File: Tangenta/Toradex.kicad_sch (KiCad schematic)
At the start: 20 parts, among them J17 2309410-1, J30 Conn_01x02_Pin, J31 Conn_01x09_Pin, J32 Conn_02x03_Odd_Even, Q3 BSS138, T1 NTZD3154NT1G

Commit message: Headers.
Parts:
- added J33, J34: Conn_01x05_Pin, Connector_PinHeader_2.54mm:PinHeader_1x05_P2.54mm_Vertical, symbol Connector:Conn_01x05_Pin
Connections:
- net GNDREF: now also J33.1 (Pin_1), J34.1 (Pin_1)
- net SPI_1_CLK: now reaches J17.196
- net SPI_1_CLK: now also J33.2 (Pin_2)
- net SPI_1_MISO: now reaches J17.198
- net SPI_1_MISO: now also J33.3 (Pin_3)
- net SPI_1_MOSI: now reaches J17.200
- net SPI_1_MOSI: now also J33.4 (Pin_4)
- net SPI_1_CS: now reaches J17.202
- net SPI_1_CS: now also J33.5 (Pin_5)
- net GPIO_1: now reaches J17.206
- net GPIO_1: now also J34.2 (Pin_2)
- net GPIO_2: now reaches J17.208
- net GPIO_2: now also J34.3 (Pin_3)
- net GPIO_3: now reaches J17.210
- net GPIO_3: now also J34.4 (Pin_4)
- net GPIO_4: now reaches J17.212
- net GPIO_4: now also J34.5 (Pin_5)
- no-connect marks 167 -> 159

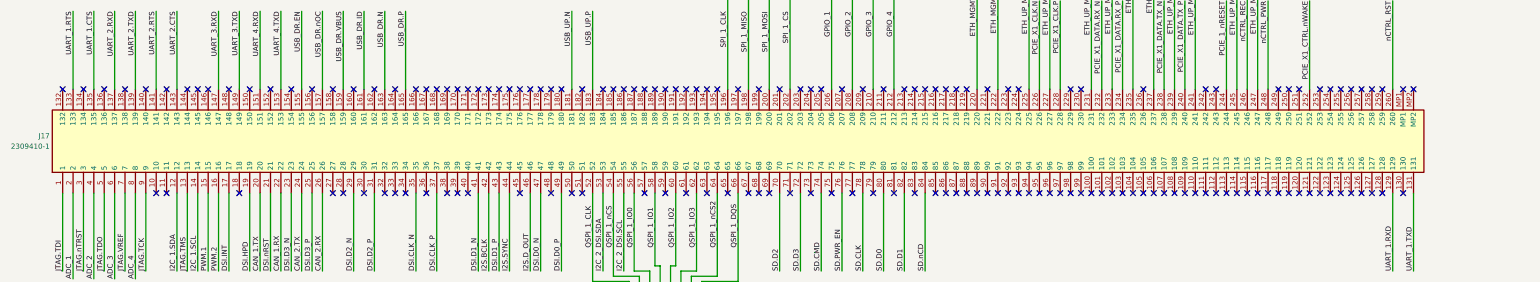
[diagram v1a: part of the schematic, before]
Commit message: SoM power and GND schematic and routing, TBD: power planes
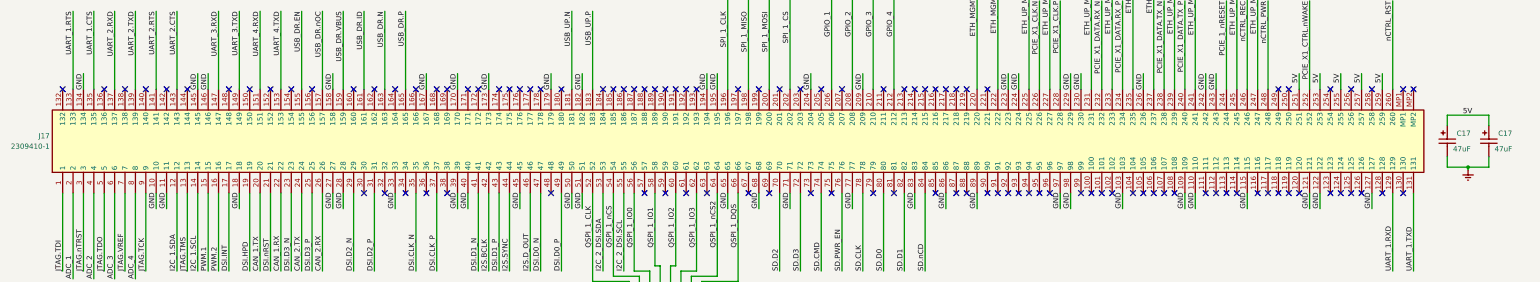
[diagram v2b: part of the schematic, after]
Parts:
- added C17 (x2): 47uF, CAP_TANTAL_A:CAP_TANTAL_A, symbol CAP_TANTAL_A:CA45-A-6_3V-47UF-K
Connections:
- net 5V: now also J17.251, J17.253, J17.255, J17.257, J17.259, C17.1, C17.1
- net GNDREF: now also J17.10, J17.103, J17.109, J17.11, J17.110, J17.115, J17.121, J17.122, J17.127, J17.134, J17.145, J17.146, J17.158, J17.167, J17.170, J17.173, J17.179, J17.18, J17.182, J17.194, J17.195, J17.204, J17.209, J17.223, J17.224, J17.229, J17.230, J17.236, J17.242, J17.243, J17.27, J17.28, J17.33, J17.39, J17.40, J17.45, J17.50, J17.51, J17.65, J17.68, J17.71, J17.77, J17.83, J17.86, J17.89, J17.97, J17.98, C17.2, C17.2
- no-connect marks 159 -> 107

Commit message: Libraries exported from global to project.
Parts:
- C17: symbol CAP_TANTAL_A:CA45-A-6_3V-47UF-K -> CholaSymbolsPrjLib:CA45-A-6_3V-47UF-K
- H15, H16, H17, H18: symbol Mechanical:MountingHole -> CholaSymbolsPrjLib:MountingHole
- J17: symbol SODIMM_DDR4:2309410-1 -> CholaSymbolsPrjLib:2309410-1
- J30: symbol Connector:Conn_01x02_Pin -> CholaSymbolsPrjLib:Conn_01x02_Pin
- J31: symbol Connector:Conn_01x09_Pin -> CholaSymbolsPrjLib:Conn_01x09_Pin
- J32: symbol Connector_Generic:Conn_02x03_Odd_Even -> CholaSymbolsPrjLib:Conn_02x03_Odd_Even
- J33, J34: symbol Connector:Conn_01x05_Pin -> CholaSymbolsPrjLib:Conn_01x05_Pin
- Q3: symbol Transistor_FET:BSS138 -> CholaSymbolsPrjLib:BSS138
- R2: symbol Device:R_Small_US -> CholaSymbolsPrjLib:R_Small_US
- T1: symbol NTZD3154NT1G:NTZD3154NT1G -> CholaSymbolsPrjLib:NTZD3154NT1G
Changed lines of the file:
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@@
     (effects (font (size 1.27 1.27)) (justify left))
   )
-  (symbol (lib_id "Device:R_Small_US") (at 289.56 72.39 180) (unit 1)
+  (symbol (lib_id "CholaSymbolsPrjLib:R_Small_US") (at 289.56 72.39 180) (unit 1)
     (in_bom yes) (on_board yes) (dnp no)
     (property "Reference" "R2" (at 288.29 71.12 0)
@@
     )
   )
-  (symbol (lib_id "Mechanical:MountingHole") (at 281.94 260.35 0) (unit 1)
+  (symbol (lib_id "CholaSymbolsPrjLib:MountingHole") (at 281.94 260.35 0) (unit 1)
     (in_bom yes) (on_board yes) (dnp no)
     (property "Reference" "H15" (at 284.48 260.35 0)
@@
     )
   )
-  (symbol (lib_id "Transistor_FET:BSS138") (at 62.23 246.38 270) (unit 1)
+  (symbol (lib_id "CholaSymbolsPrjLib:BSS138") (at 62.23 246.38 270) (unit 1)
     (in_bom yes) (on_board yes) (dnp no)
     (property "Reference" "Q3" (at 64.77 243.84 90)
@@
     )
   )
-  (symbol (lib_id "Mechanical:MountingHole") (at 281.94 275.59 0) (unit 1)
+  (symbol (lib_id "CholaSymbolsPrjLib:MountingHole") (at 281.94 275.59 0) (unit 1)
     (in_bom yes) (on_board yes) (dnp no)
     (property "Reference" "H18" (at 284.48 275.59 0)
@@
     )
   )
-  (symbol (lib_id "Device:R_Small_US") (at 49.53 242.57 180) (unit 1)
+  (symbol (lib_id "CholaSymbolsPrjLib:R_Small_US") (at 49.53 242.57 180) (unit 1)
     (in_bom yes) (on_board yes) (dnp no)
     (property "Reference" "R2" (at 48.26 241.3 0)
@@
     )
   )
-  (symbol (lib_id "Connector:Conn_01x02_Pin") (at 344.805 77.47 90) (mirror x) (unit 1)
+  (symbol (lib_id "CholaSymbolsPrjLib:Conn_01x02_Pin") (at 344.805 77.47 90) (mirror x) (unit 1)
     (in_bom yes) (on_board yes) (dnp no)
     (property "Reference" "J30" (at 344.17 76.2 90)
@@
     )
   )
-  (symbol (lib_id "Mechanical:MountingHole") (at 281.94 265.43 0) (unit 1)
+  (symbol (lib_id "CholaSymbolsPrjLib:MountingHole") (at 281.94 265.43 0) (unit 1)
     (in_bom yes) (on_board yes) (dnp no)
     (property "Reference" "H16" (at 284.48 265.43 0)
@@
     )
   )
-  (symbol (lib_id "SODIMM_DDR4:2309410-1") (at 49.53 148.59 90) (unit 1)
+  (symbol (lib_id "CholaSymbolsPrjLib:2309410-1") (at 49.53 148.59 90) (unit 1)
     (in_bom yes) (on_board yes) (dnp no) (fields_autoplaced)
     (property "Reference" "J17" (at 46.355 134.62 90)
@@
     )
   )
-  (symbol (lib_id "Device:R_Small_US") (at 76.2 242.57 180) (unit 1)
+  (symbol (lib_id "CholaSymbolsPrjLib:R_Small_US") (at 76.2 242.57 180) (unit 1)
     (in_bom yes) (on_board yes) (dnp no)
     (property "Reference" "R2" (at 74.93 241.3 0)
@@
     )
   )
-  (symbol (lib_id "Connector:Conn_01x09_Pin") (at 198.12 177.165 270) (mirror x) (unit 1)
+  (symbol (lib_id "CholaSymbolsPrjLib:Conn_01x09_Pin") (at 198.12 177.165 270) (mirror x) (unit 1)
     (in_bom no) (on_board yes) (dnp yes)
     (property "Reference" "J31" (at 210.82 174.625 90)
@@
     )
   )
-  (symbol (lib_id "Device:R_Small_US") (at 49.53 266.7 180) (unit 1)
+  (symbol (lib_id "CholaSymbolsPrjLib:R_Small_US") (at 49.53 266.7 180) (unit 1)
     (in_bom yes) (on_board yes) (dnp no)
     (property "Reference" "R2" (at 48.26 265.43 0)
@@
     )
   )
-  (symbol (lib_id "CAP_TANTAL_A:CA45-A-6_3V-47UF-K") (at 387.985 135.89 270) (mirror x) (unit 1)
+  (symbol (lib_id "CholaSymbolsPrjLib:CA45-A-6_3V-47UF-K") (at 387.985 135.89 270) (mirror x) (unit 1)
     (in_bom yes) (on_board yes) (dnp no)
     (property "Reference" "C17" (at 393.7 133.985 90)
@@
     )
   )
-  (symbol (lib_id "NTZD3154NT1G:NTZD3154NT1G") (at 298.45 68.58 0) (unit 1)
+  (symbol (lib_id "CholaSymbolsPrjLib:NTZD3154NT1G") (at 298.45 68.58 0) (unit 1)
     (in_bom yes) (on_board yes) (dnp no)
     (property "Reference" "T1" (at 299.085 64.77 0)
@@
     )
   )
-  (symbol (lib_id "Connector:Conn_01x05_Pin") (at 217.17 90.17 90) (mirror x) (unit 1)
+  (symbol (lib_id "CholaSymbolsPrjLib:Conn_01x05_Pin") (at 217.17 90.17 90) (mirror x) (unit 1)
     (in_bom no) (on_board yes) (dnp yes)
     (property "Reference" "J33" (at 217.17 88.9 90)
@@
     )
   )
-  (symbol (lib_id "Device:R_Small_US") (at 298.45 58.42 180) (unit 1)
+  (symbol (lib_id "CholaSymbolsPrjLib:R_Small_US") (at 298.45 58.42 180) (unit 1)
     (in_bom yes) (on_board yes) (dnp no)
     (property "Reference" "R2" (at 297.18 57.15 0)
@@
     )
   )
-  (symbol (lib_id "NTZD3154NT1G:NTZD3154NT1G") (at 316.23 68.58 0) (unit 2)
+  (symbol (lib_id "CholaSymbolsPrjLib:NTZD3154NT1G") (at 316.23 68.58 0) (unit 2)
     (in_bom yes) (on_board yes) (dnp no)
     (property "Reference" "T1" (at 316.865 64.77 0)
@@
     )
   )
-  (symbol (lib_id "CAP_TANTAL_A:CA45-A-6_3V-47UF-K") (at 398.145 135.89 270) (mirror x) (unit 1)
+  (symbol (lib_id "CholaSymbolsPrjLib:CA45-A-6_3V-47UF-K") (at 398.145 135.89 270) (mirror x) (unit 1)
     (in_bom yes) (on_board yes) (dnp no)
     (property "Reference" "C17" (at 403.86 133.985 90)
@@
     )
   )
-  (symbol (lib_id "Connector_Generic:Conn_02x03_Odd_Even") (at 58.42 177.8 0) (unit 1)
+  (symbol (lib_id "CholaSymbolsPrjLib:Conn_02x03_Odd_Even") (at 58.42 177.8 0) (unit 1)
     (in_bom no) (on_board yes) (dnp yes)
     (property "Reference" "J32" (at 59.69 172.72 0)
@@
     )
   )
-  (symbol (lib_id "Device:R_Small_US") (at 76.2 266.7 180) (unit 1)
+  (symbol (lib_id "CholaSymbolsPrjLib:R_Small_US") (at 76.2 266.7 180) (unit 1)
     (in_bom yes) (on_board yes) (dnp no)
     (property "Reference" "R2" (at 74.93 265.43 0)
@@
     )
   )
-  (symbol (lib_id "Transistor_FET:BSS138") (at 62.23 270.51 270) (unit 1)
+  (symbol (lib_id "CholaSymbolsPrjLib:BSS138") (at 62.23 270.51 270) (unit 1)
     (in_bom yes) (on_board yes) (dnp no)
     (property "Reference" "Q3" (at 64.77 267.97 90)
@@
     )
   )
-  (symbol (lib_id "Device:R_Small_US") (at 339.09 86.995 180) (unit 1)
+  (symbol (lib_id "CholaSymbolsPrjLib:R_Small_US") (at 339.09 86.995 180) (unit 1)
     (in_bom yes) (on_board yes) (dnp no)
     (property "Reference" "R2" (at 337.82 85.725 0)
@@
     )
   )
-  (symbol (lib_id "Device:R_Small_US") (at 332.74 55.88 180) (unit 1)
+  (symbol (lib_id "CholaSymbolsPrjLib:R_Small_US") (at 332.74 55.88 180) (unit 1)
     (in_bom yes) (on_board yes) (dnp no)
     (property "Reference" "R2" (at 331.47 54.61 0)
@@
     )
   )
-  (symbol (lib_id "Device:R_Small_US") (at 316.23 58.42 180) (unit 1)
+  (symbol (lib_id "CholaSymbolsPrjLib:R_Small_US") (at 316.23 58.42 180) (unit 1)
     (in_bom yes) (on_board yes) (dnp no)
     (property "Reference" "R2" (at 314.96 57.15 0)
@@
     )
   )
-  (symbol (lib_id "Connector:Conn_01x05_Pin") (at 242.57 90.17 90) (mirror x) (unit 1)
+  (symbol (lib_id "CholaSymbolsPrjLib:Conn_01x05_Pin") (at 242.57 90.17 90) (mirror x) (unit 1)
     (in_bom no) (on_board yes) (dnp yes)
     (property "Reference" "J34" (at 242.57 88.9 90)
@@
     )
   )
-  (symbol (lib_id "Mechanical:MountingHole") (at 281.94 270.51 0) (unit 1)
+  (symbol (lib_id "CholaSymbolsPrjLib:MountingHole") (at 281.94 270.51 0) (unit 1)
     (in_bom yes) (on_board yes) (dnp no)
     (property "Reference" "H17" (at 284.48 270.51 0)
